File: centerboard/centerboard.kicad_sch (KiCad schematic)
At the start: 12 parts, among them J1 Conn_01x10_MountingPin, U1 ProMicro

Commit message: redo centerboard again (and again)
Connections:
- net COL_L1: now also U1.2 (RX); no longer U1.19 (F5)
- net COL_L2: now also U1.6 (SCL); no longer U1.12 (B5)
- net COL_L3: now also U1.8 (C6); no longer U1.6 (SCL)
- net COL_R1: now also U1.20 (F4); no longer U1.13 (B6)
- net COL_R2: now also U1.19 (F5); no longer U1.20 (F4)
- net COL_R3: now also U1.14 (B2); no longer U1.11 (B4)
- net COL_T: now also U1.11 (B4); no longer U1.14 (B2)
- net ROW_1: now also U1.1 (TX); no longer U1.7 (D4)
- net ROW_2: now also U1.18 (F6); no longer U1.8 (C6)
- net ROW_3: now also U1.5 (SDA); no longer U1.9 (D7)
- net ROW_4: now also U1.9 (D7); no longer U1.10 (E6)
- net ROW_5: now also U1.16 (B1); no longer U1.18 (F6)
- net ROW_7: now also U1.7 (D4); no longer U1.16 (B1)
- net ROW_8: now also U1.10 (E6); no longer U1.15 (B3)
- net SGCLK: now also U1.15 (B3); no longer U1.2 (RX)
- net SGDX: now also U1.13 (B6); no longer U1.1 (TX)
- net SGDY: now also U1.12 (B5); no longer U1.5 (SDA)

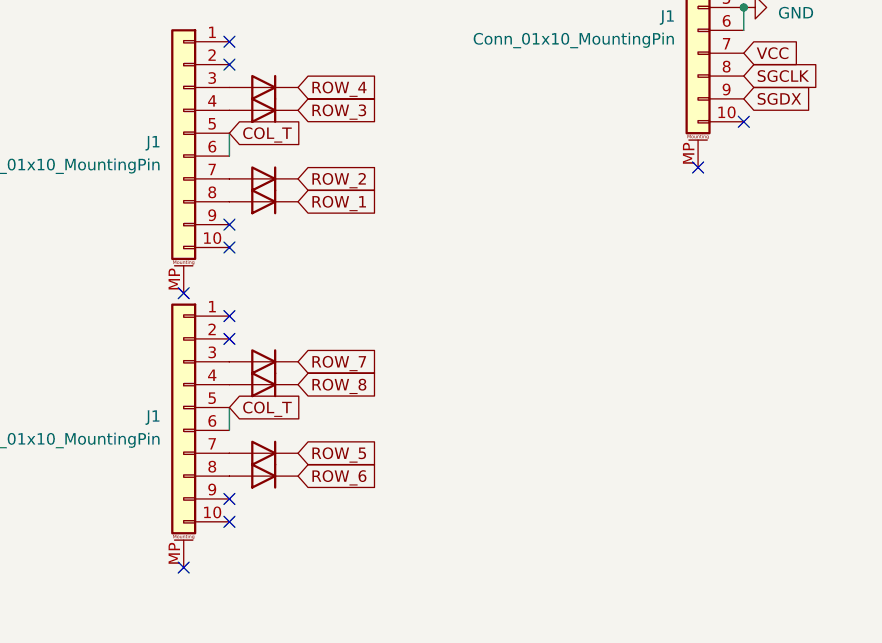
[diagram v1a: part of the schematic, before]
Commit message: Rework centerboard yet again. Now with vertical FFC headers and a ground pour.
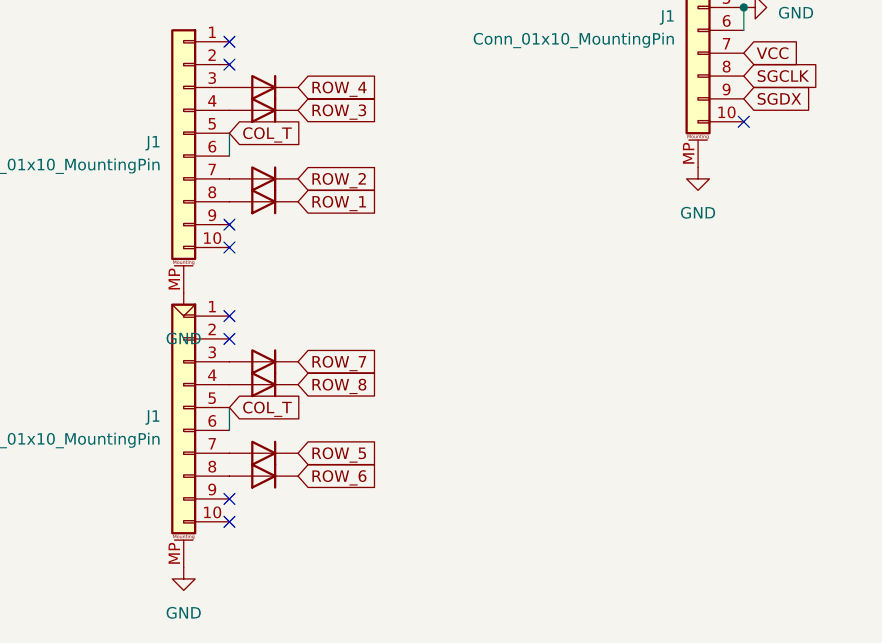
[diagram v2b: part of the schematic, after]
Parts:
- J1: footprint Custom:FFC_Clamshell_0.5mm_1x10 -> Custom:GCT_FFC2A33-10-T-R_REVA
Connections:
- net GND: now also J1.MP (MountPin), J1.MP (MountPin), J1.MP (MountPin)
- no-connect marks 17 -> 14
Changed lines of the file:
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@@
   (junction (at 147.32 132.08) (diameter 0) (color 0 0 0 0)
   )
-  (no_connect (at 142.24 149.86))
-  (no_connect (at 85.09 194.31))
   (no_connect (at 147.32 144.78))
   (no_connect (at 90.17 135.89))
@@
   (no_connect (at 90.17 138.43))
   (no_connect (at 90.17 189.23))
-  (no_connect (at 85.09 163.83))
   (no_connect (at 147.32 121.92))
   (no_connect (at 90.17 166.37))
@@
       (effects (font (size 1.27 1.27)) (justify left))
     )
-    (property "Footprint" "Custom:FFC_Clamshell_0.5mm_1x10" (at 142.24 132.08 0)
+    (property "Footprint" "Custom:GCT_FFC2A33-10-T-R_REVA" (at 142.24 132.08 0)
       (effects (font (size 1.27 1.27)) hide)
     )
@@
     )
   )
+  (symbol (lib_id "power:GND") (at 85.09 163.83 0) (unit 1)
+    (in_bom yes) (on_board yes) (dnp no) (fields_autoplaced)
+    (property "Reference" "#PWR04" (at 85.09 170.18 0)
+      (effects (font (size 1.27 1.27)) hide)
+    )
+    (property "Value" "GND" (at 85.09 168.91 0)
+      (effects (font (size 1.27 1.27)))
+    )
+    (property "Footprint" "" (at 85.09 163.83 0)
+      (effects (font (size 1.27 1.27)) hide)
+    )
+    (property "Datasheet" "" (at 85.09 163.83 0)
+      (effects (font (size 1.27 1.27)) hide)
+    )
+    (pin "1")
+    (instances
+      (project "centerboard"
+        (path "/4cf5c873-f5e9-4261-911c-886f387fb0f3"
+          (reference "#PWR04") (unit 1)
+        )
+      )
+    )
+  )
   (symbol (lib_id "Diode:1N4148W") (at 93.98 153.67 180) (unit 1)
     (in_bom yes) (on_board yes) (dnp no) (fields_autoplaced)
@@
       (effects (font (size 1.27 1.27)) (justify left))
     )
-    (property "Footprint" "Custom:FFC_Clamshell_0.5mm_1x10" (at 85.09 176.53 0)
+    (property "Footprint" "Custom:GCT_FFC2A33-10-T-R_REVA" (at 85.09 176.53 0)
       (effects (font (size 1.27 1.27)) hide)
     )
@@
       (effects (font (size 1.27 1.27)) (justify left))
     )
-    (property "Footprint" "Custom:FFC_Clamshell_0.5mm_1x10" (at 85.09 146.05 0)
+    (property "Footprint" "Custom:GCT_FFC2A33-10-T-R_REVA" (at 85.09 146.05 0)
       (effects (font (size 1.27 1.27)) hide)
     )
@@
         (path "/4cf5c873-f5e9-4261-911c-886f387fb0f3/e4834520-9e93-41c6-9dec-c6197700f3e4"
           (reference "D43") (unit 1)
+        )
+      )
+    )
+  )
+  (symbol (lib_id "power:GND") (at 85.09 194.31 0) (unit 1)
+    (in_bom yes) (on_board yes) (dnp no) (fields_autoplaced)
+    (property "Reference" "#PWR03" (at 85.09 200.66 0)
+      (effects (font (size 1.27 1.27)) hide)
+    )
+    (property "Value" "GND" (at 85.09 199.39 0)
+      (effects (font (size 1.27 1.27)))
+    )
+    (property "Footprint" "" (at 85.09 194.31 0)
+      (effects (font (size 1.27 1.27)) hide)
+    )
+    (property "Datasheet" "" (at 85.09 194.31 0)
+      (effects (font (size 1.27 1.27)) hide)
+    )
+    (pin "1")
+    (instances
+      (project "centerboard"
+        (path "/4cf5c873-f5e9-4261-911c-886f387fb0f3"
+          (reference "#PWR03") (unit 1)
         )
       )
@@
         )
       )
+    )
+  )
+  (symbol (lib_id "power:GND") (at 142.24 149.86 0) (unit 1)
+    (in_bom yes) (on_board yes) (dnp no) (fields_autoplaced)
+    (property "Reference" "#PWR05" (at 142.24 156.21 0)
+      (effects (font (size 1.27 1.27)) hide)
+    )
+    (property "Value" "GND" (at 142.24 154.94 0)
+      (effects (font (size 1.27 1.27)))
+    )
+    (property "Footprint" "" (at 142.24 149.86 0)
+      (effects (font (size 1.27 1.27)) hide)
+    )
+    (property "Datasheet" "" (at 142.24 149.86 0)
+      (effects (font (size 1.27 1.27)) hide)
+    )
+    (pin "1")
+    (instances
+      (project "centerboard"
+        (path "/4cf5c873-f5e9-4261-911c-886f387fb0f3"
+          (reference "#PWR05") (unit 1)
+        )
+      )
